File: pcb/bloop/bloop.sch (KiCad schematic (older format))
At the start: 3 parts

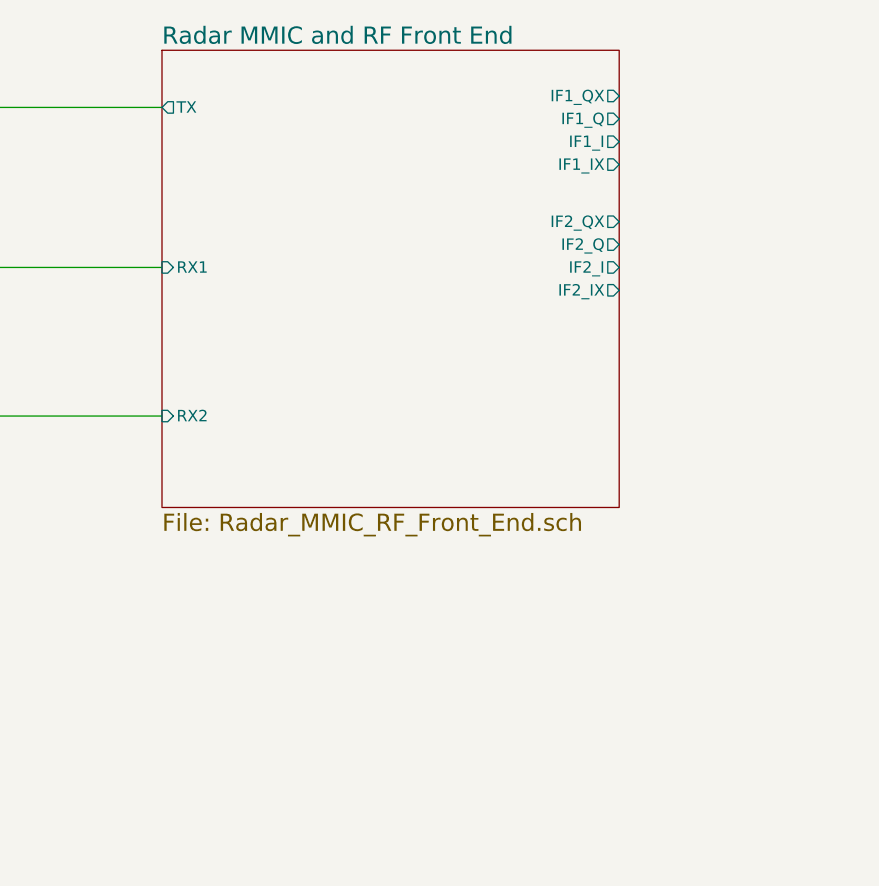
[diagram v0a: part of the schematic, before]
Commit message: Started PLL circuitry Added PLL device and oscillator Still need loop filter and clock filter circuits
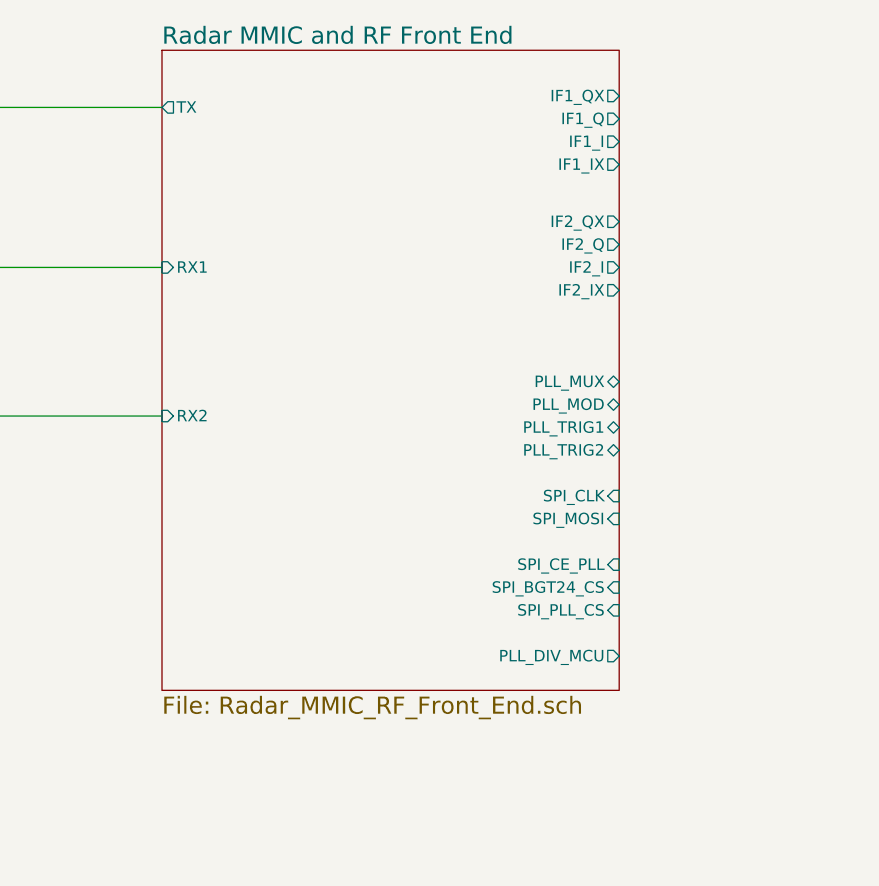
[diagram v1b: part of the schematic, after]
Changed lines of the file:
@@
 	3100 5000 3900 5000
 $Sheet
-S 3900 3400 2000 2000
+S 3900 3400 2000 2800
 U 5D3D1628
 F0 "Radar MMIC and RF Front End" 75
@@
 F11 "IF2_I" O R 5900 4350 50
 F12 "IF2_IX" O R 5900 4450 50
+F13 "SPI_CE_PLL" I R 5900 5650 50
+F14 "SPI_CLK" I R 5900 5350 50
+F15 "SPI_MOSI" I R 5900 5450 50
+F16 "SPI_PLL_CS" I R 5900 5850 50
+F17 "PLL_MOD" B R 5900 4950 50
+F18 "PLL_TRIG1" B R 5900 5050 50
+F19 "PLL_TRIG2" B R 5900 5150 50
+F20 "PLL_MUX" B R 5900 4850 50
+F21 "PLL_DIV_MCU" O R 5900 6050 50
+F22 "SPI_BGT24_CS" I R 5900 5750 50
 $EndSheet
 $EndSCHEMATC

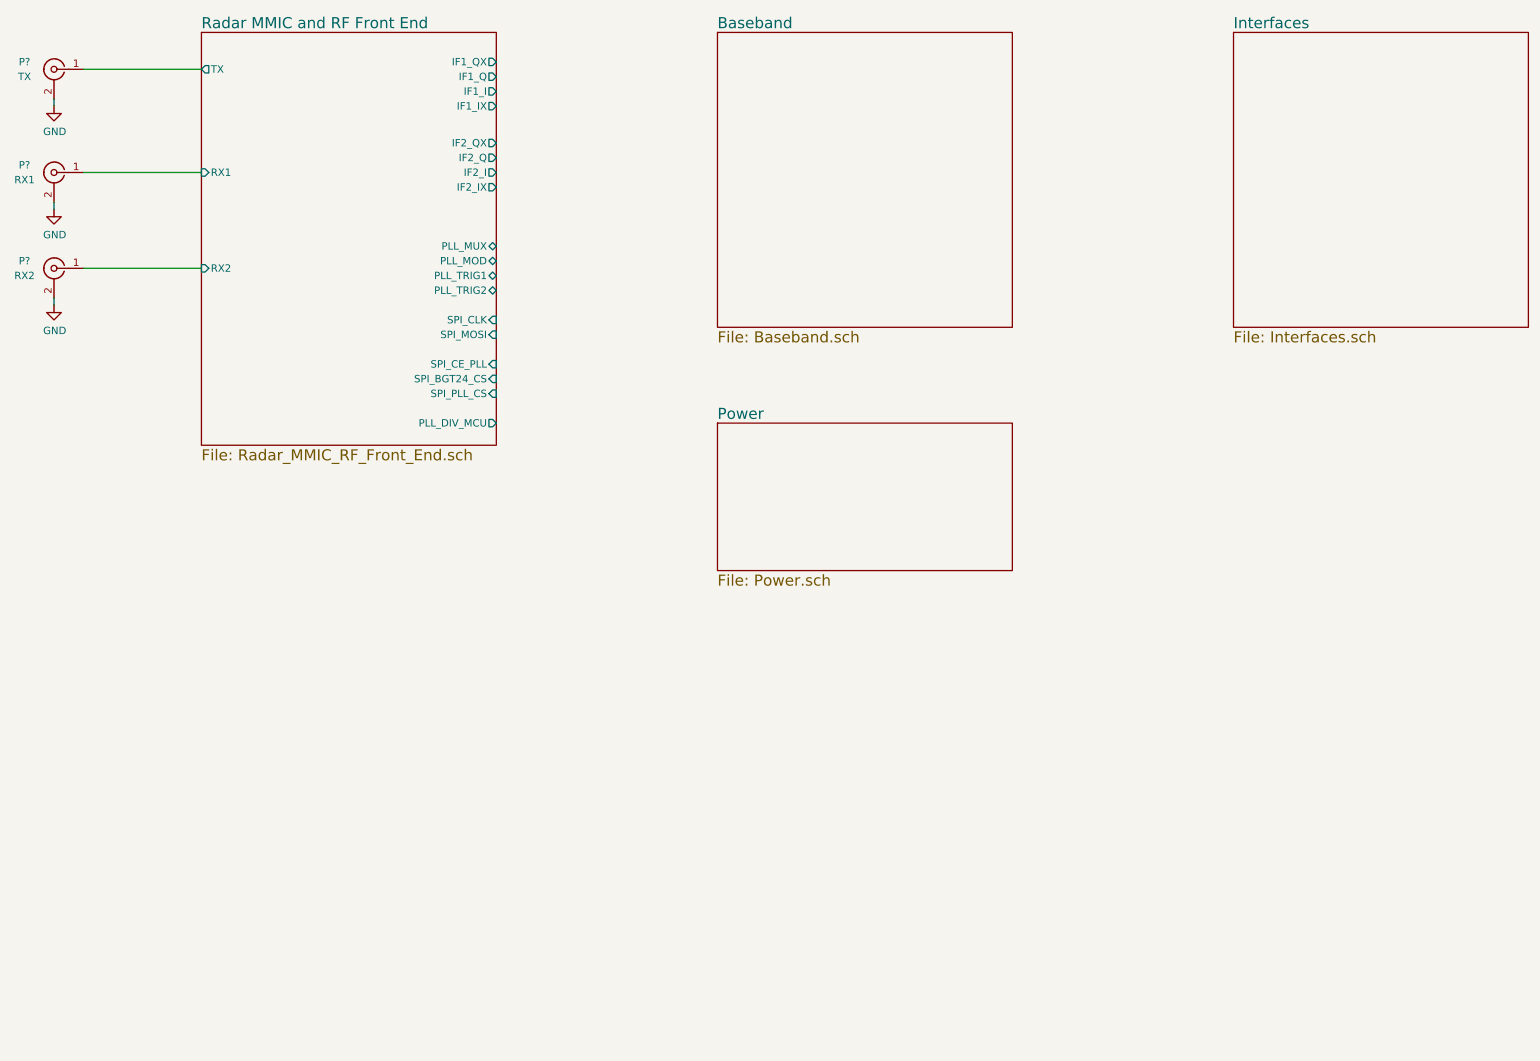
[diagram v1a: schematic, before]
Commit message: Add DC blocking capacitors; add larger resistor and capacitor symbols; implement root PN for symbols
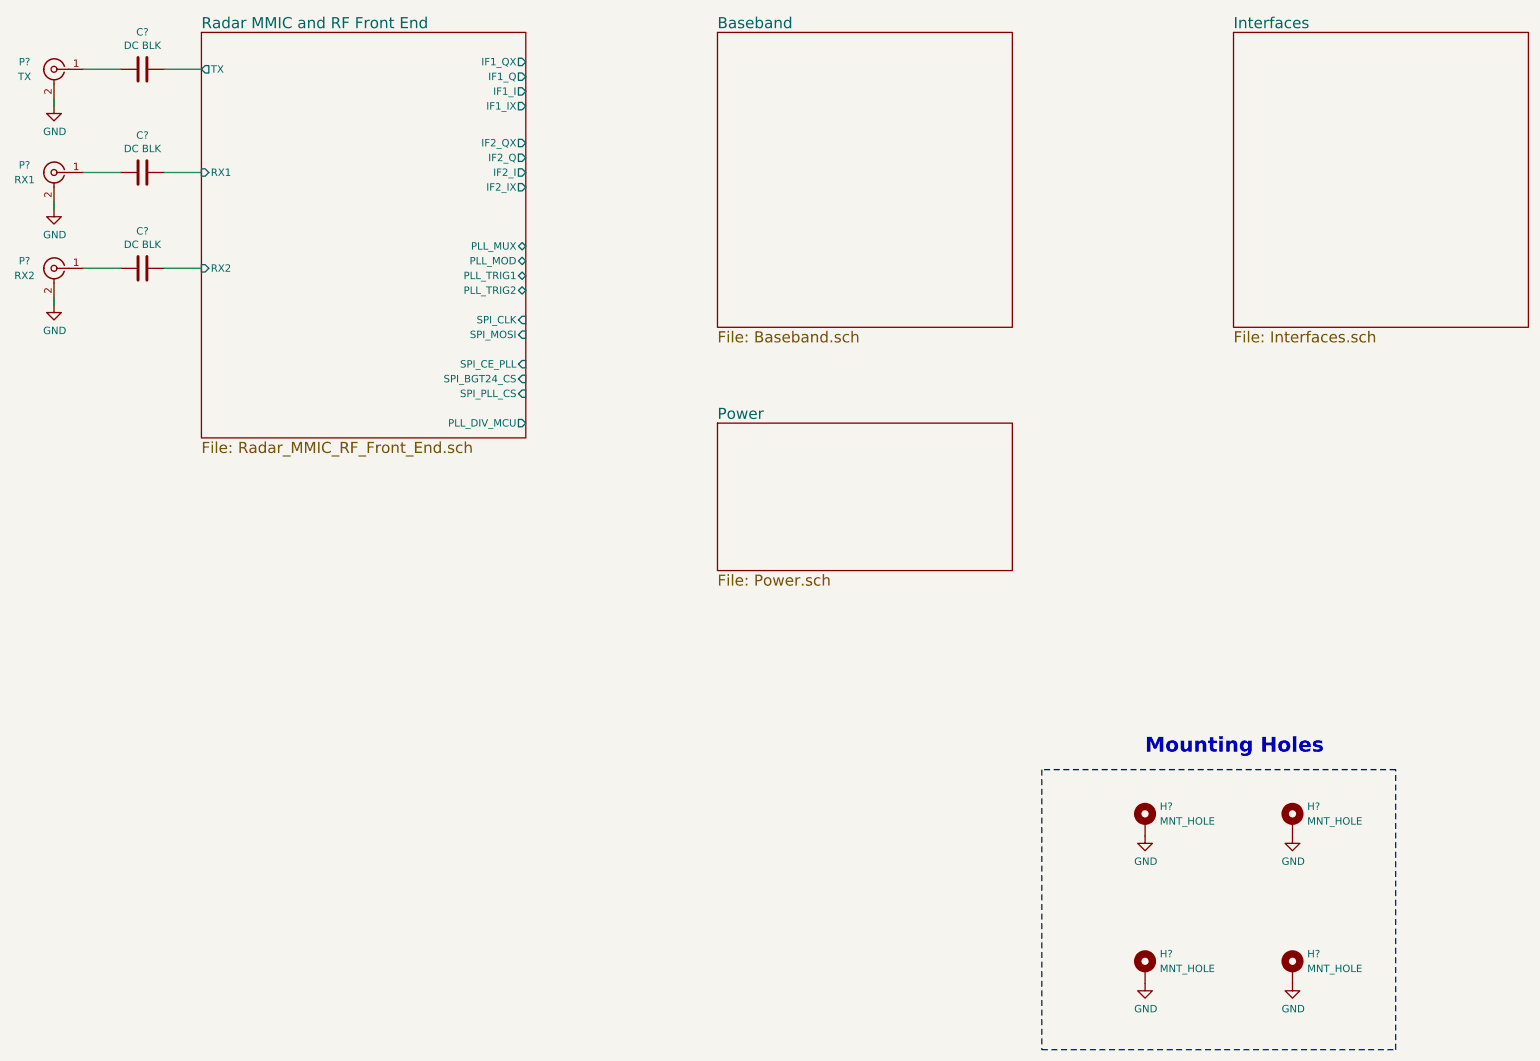
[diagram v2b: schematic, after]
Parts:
- added C? (x3): DC BLK, symbol Device:C
- added H? (x4): MNT_HOLE, symbol Mechanical:MountingHole_Pad
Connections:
- net GND: now also H?.1, H?.1, H?.1, H?.1
- net Radar MMIC and RF Front End/RX1: now also C?.1; no longer P?.1 (In)
- net Radar MMIC and RF Front End/RX2: now also C?.1; no longer P?.1 (In)
- net Radar MMIC and RF Front End/TX: now also C?.1; no longer P?.1 (In)
- new net: C?.2, P?.1 (In) (x3)
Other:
- note added: "Mounting Holes"
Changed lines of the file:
@@
 	1    0    0    -1
 $EndComp
-Wire Wire Line
-	3100 3650 3900 3650
-Wire Wire Line
-	3100 4350 3900 4350
-Wire Wire Line
-	3100 5000 3900 5000
 $Sheet
-S 3900 3400 2000 2800
+S 3900 3400 2200 2750
 U 5D3D1628
 F0 "Radar MMIC and RF Front End" 75
@@
 F3 "RX1" I L 3900 4350 50
 F4 "RX2" I L 3900 5000 50
-F5 "IF1_QX" O R 5900 3600 50
-F6 "IF1_Q" O R 5900 3700 50
-F7 "IF1_I" O R 5900 3800 50
-F8 "IF1_IX" O R 5900 3900 50
-F9 "IF2_QX" O R 5900 4150 50
-F10 "IF2_Q" O R 5900 4250 50
-F11 "IF2_I" O R 5900 4350 50
-F12 "IF2_IX" O R 5900 4450 50
-F13 "SPI_CE_PLL" I R 5900 5650 50
-F14 "SPI_CLK" I R 5900 5350 50
-F15 "SPI_MOSI" I R 5900 5450 50
-F16 "SPI_PLL_CS" I R 5900 5850 50
-F17 "PLL_MOD" B R 5900 4950 50
-F18 "PLL_TRIG1" B R 5900 5050 50
-F19 "PLL_TRIG2" B R 5900 5150 50
-F20 "PLL_MUX" B R 5900 4850 50
-F21 "PLL_DIV_MCU" O R 5900 6050 50
-F22 "SPI_BGT24_CS" I R 5900 5750 50
+F5 "IF1_QX" O R 6100 3600 50
+F6 "IF1_Q" O R 6100 3700 50
+F7 "IF1_I" O R 6100 3800 50
+F8 "IF1_IX" O R 6100 3900 50
+F9 "IF2_QX" O R 6100 4150 50
+F10 "IF2_Q" O R 6100 4250 50
+F11 "IF2_I" O R 6100 4350 50
+F12 "IF2_IX" O R 6100 4450 50
+F13 "SPI_CE_PLL" I R 6100 5650 50
+F14 "SPI_CLK" I R 6100 5350 50
+F15 "SPI_MOSI" I R 6100 5450 50
+F16 "SPI_PLL_CS" I R 6100 5850 50
+F17 "PLL_MOD" B R 6100 4950 50
+F18 "PLL_TRIG1" B R 6100 5050 50
+F19 "PLL_TRIG2" B R 6100 5150 50
+F20 "PLL_MUX" B R 6100 4850 50
+F21 "PLL_DIV_MCU" O R 6100 6050 50
+F22 "SPI_BGT24_CS" I R 6100 5750 50
 $EndSheet
+$Comp
+L Device:C C?
+U 1 1 5D454FFB
+P 3500 3650
+AR Path="/5D3D1628/5D454FFB" Ref="C?"  Part="1"
+AR Path="/5D454FFB" Ref="C?"  Part="1"
+F 0 "C?" V 3248 3650 50  0000 C CNN
+F 1 "DC BLK" V 3339 3650 50  0000 C CNN
+F 2 "" H 3538 3500 50  0001 C CNN
+F 3 "~" H 3500 3650 50  0001 C CNN
+	1    3500 3650
+	0    1    1    0
+$EndComp
+Wire Wire Line
+	3900 3650 3650 3650
+Wire Wire Line
+	3350 3650 3100 3650
+$Comp
+L Device:C C?
+U 1 1 5D455B2F
+P 3500 4350
+AR Path="/5D3D1628/5D455B2F" Ref="C?"  Part="1"
+AR Path="/5D455B2F" Ref="C?"  Part="1"
+F 0 "C?" V 3248 4350 50  0000 C CNN
+F 1 "DC BLK" V 3339 4350 50  0000 C CNN
+F 2 "" H 3538 4200 50  0001 C CNN
+F 3 "~" H 3500 4350 50  0001 C CNN
+	1    3500 4350
+	0    1    1    0
+$EndComp
+Wire Wire Line
+	3900 4350 3650 4350
+Wire Wire Line
+	3350 4350 3100 4350
+$Comp
+L Device:C C?
+U 1 1 5D455FA2
+P 3500 5000
+AR Path="/5D3D1628/5D455FA2" Ref="C?"  Part="1"
+AR Path="/5D455FA2" Ref="C?"  Part="1"
+F 0 "C?" V 3248 5000 50  0000 C CNN
+F 1 "DC BLK" V 3339 5000 50  0000 C CNN
+F 2 "" H 3538 4850 50  0001 C CNN
+F 3 "~" H 3500 5000 50  0001 C CNN
+	1    3500 5000
+	0    1    1    0
+$EndComp
+Wire Wire Line
+	3900 5000 3650 5000
+Wire Wire Line
+	3350 5000 3100 5000
+$Comp
+L Mechanical:MountingHole_Pad H?
+U 1 1 5D89D33B
+P 11300 9750
+F 0 "H?" H 11400 9850 50  0000 L CNN
+F 1 "MNT_HOLE" H 11400 9750 50  0000 L CNN
+F 2 "" H 11300 9750 50  0001 C CNN
+F 3 "~" H 11300 9750 50  0001 C CNN
+	1    11300 9750
+	1    0    0    -1
+$EndComp
+$Comp
+L power:GND #PWR?
+U 1 1 5D89E2C2
+P 11300 9850
+F 0 "#PWR?" H 11300 9600 50  0001 C CNN
+F 1 "GND" H 11305 9677 50  0000 C CNN
+F 2 "" H 11300 9850 50  0001 C CNN
+F 3 "" H 11300 9850 50  0001 C CNN
+	1    11300 9850
+	1    0    0    -1
+$EndComp
+$Comp
+L Mechanical:MountingHole_Pad H?
+U 1 1 5D89F708
+P 10300 9750
+F 0 "H?" H 10400 9850 50  0000 L CNN
+F 1 "MNT_HOLE" H 10400 9750 50  0000 L CNN
+F 2 "" H 10300 9750 50  0001 C CNN
+F 3 "~" H 10300 9750 50  0001 C CNN
+	1    10300 9750
+	1    0    0    -1
+$EndComp
+$Comp
+L power:GND #PWR?
+U 1 1 5D89F70E
+P 10300 9850
+F 0 "#PWR?" H 10300 9600 50  0001 C CNN
+F 1 "GND" H 10305 9677 50  0000 C CNN
+F 2 "" H 10300 9850 50  0001 C CNN
+F 3 "" H 10300 9850 50  0001 C CNN
+	1    10300 9850
+	1    0    0    -1
+$EndComp
+$Comp
+L Mechanical:MountingHole_Pad H?
+U 1 1 5D8A33A6
+P 11300 8750
+F 0 "H?" H 11400 8850 50  0000 L CNN
+F 1 "MNT_HOLE" H 11400 8750 50  0000 L CNN
+F 2 "" H 11300 8750 50  0001 C CNN
+F 3 "~" H 11300 8750 50  0001 C CNN
+	1    11300 8750
+	1    0    0    -1
+$EndComp
+$Comp
+L power:GND #PWR?
+U 1 1 5D8A33AC
+P 11300 8850
+F 0 "#PWR?" H 11300 8600 50  0001 C CNN
+F 1 "GND" H 11305 8677 50  0000 C CNN
+F 2 "" H 11300 8850 50  0001 C CNN
+F 3 "" H 11300 8850 50  0001 C CNN
+	1    11300 8850
+	1    0    0    -1
+$EndComp
+$Comp
+L Mechanical:MountingHole_Pad H?
+U 1 1 5D8A33B2
+P 10300 8750
+F 0 "H?" H 10400 8850 50  0000 L CNN
+F 1 "MNT_HOLE" H 10400 8750 50  0000 L CNN
+F 2 "" H 10300 8750 50  0001 C CNN
+F 3 "~" H 10300 8750 50  0001 C CNN
+	1    10300 8750
+	1    0    0    -1
+$EndComp
+$Comp
+L power:GND #PWR?
+U 1 1 5D8A33B8
+P 10300 8850
+F 0 "#PWR?" H 10300 8600 50  0001 C CNN
+F 1 "GND" H 10305 8677 50  0000 C CNN
+F 2 "" H 10300 8850 50  0001 C CNN
+F 3 "" H 10300 8850 50  0001 C CNN
+	1    10300 8850
+	1    0    0    -1
+$EndComp
+Wire Notes Line
+	9600 8400 9600 10300
+Wire Notes Line
+	9600 10300 12000 10300
+Wire Notes Line
+	12000 10300 12000 8400
+Wire Notes Line
+	12000 8400 9600 8400
+Text Notes 10300 8300 0    100  ~ 20
+Mounting Holes
 $EndSCHEMATC
